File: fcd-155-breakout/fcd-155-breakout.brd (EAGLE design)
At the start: 52 x 63.2 mm, 2 parts, among them X1 RJ45-8X-E5908

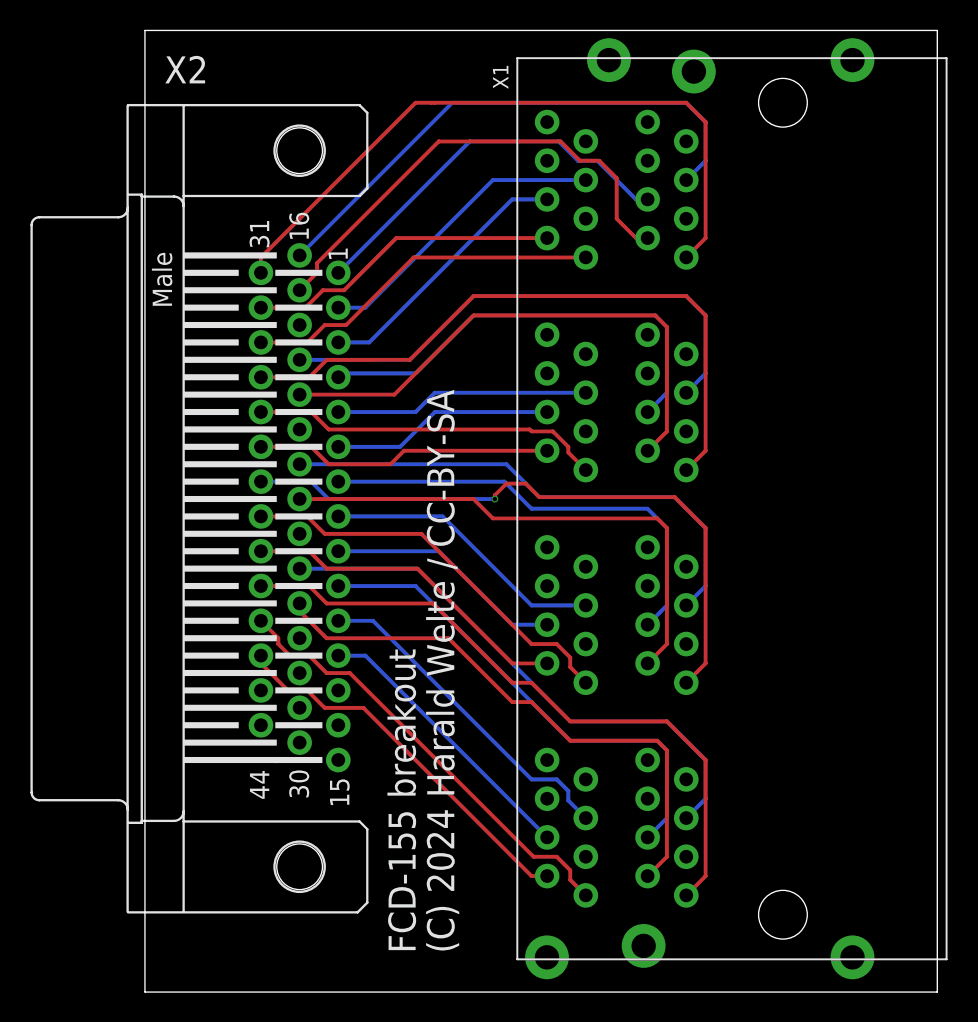
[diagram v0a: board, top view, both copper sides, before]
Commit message: fcd-155-breakout: Fix pin-out for even numbered ports
Related: OS#6678
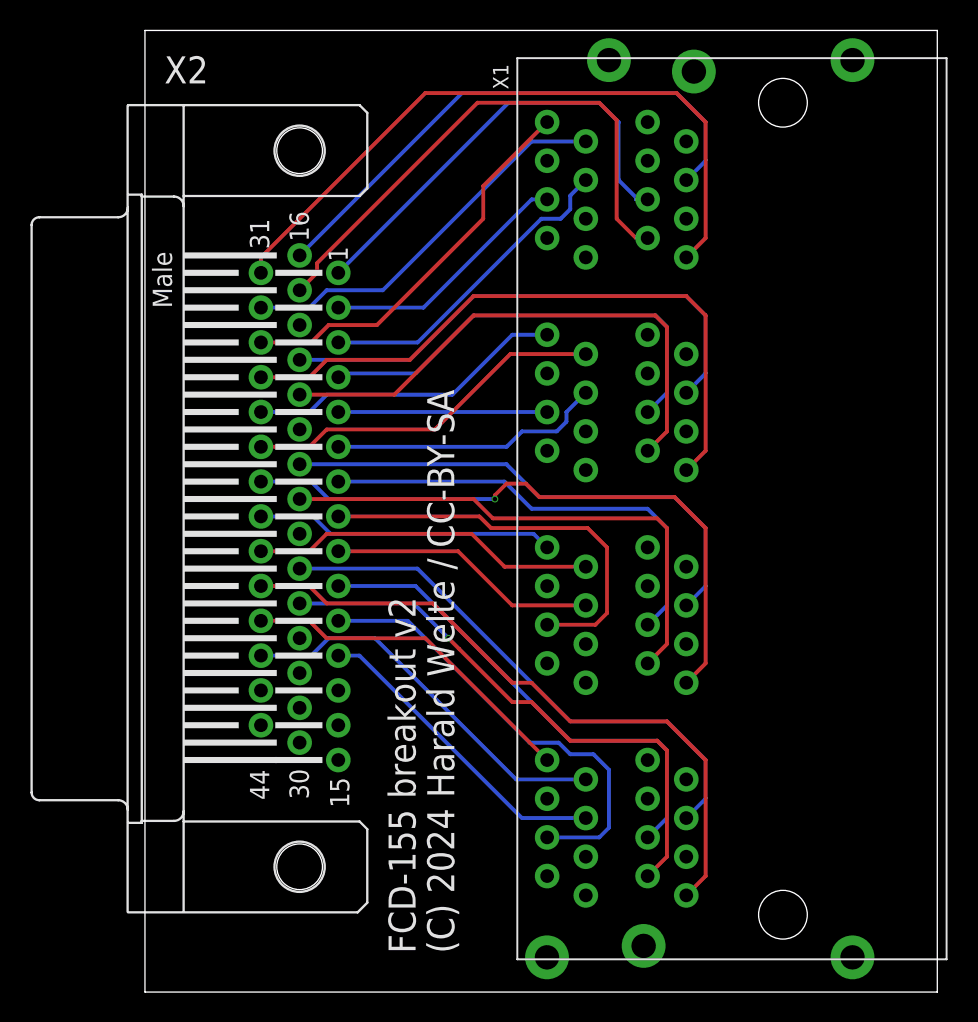
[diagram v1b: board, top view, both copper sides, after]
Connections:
- net CH2_RX_N: now also X1.D1; no longer X1.DU1
- net CH2_RX_P: now also X1.D2; no longer X1.DU2
- net CH2_TX_N: now also X1.D4; no longer X1.DU4
- net CH2_TX_P: now also X1.D5; no longer X1.DU5
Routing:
- net CH6_TX_P: track 18.7 -> 27.1 mm
- net CH8_TX_P: track 22.0 -> 30.0 mm
- net CH8_RX_N: track 29.4 -> 22.6 mm
- net CH6_RX_N: track 26.2 -> 19.6 mm
- net CH2_RX_P: track 20.7 -> 25.9 mm
- net CH1_TX_N: track 25.5 -> 29.9 mm
- net CH1_RX_P: track 31.5 -> 35.8 mm
- net CH4_RX_P: track 19.6 -> 23.9 mm
- net CH2_TX_N: track 17.6 -> 21.2 mm
- net CH4_TX_N: track 14.9 -> 18.1 mm
- net CH2_TX_P: track 19.7 -> 16.7 mm
- net CH4_TX_P: track 16.8 -> 13.7 mm
- net CH2_RX_N: track 23.7 -> 26.1 mm
- net CH4_RX_N: track 23.1 -> 20.9 mm
- net CH8_TX_N: track 18.7 -> 20.7 mm
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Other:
- board text added: "FCD-155 breakout v2"
- board text removed: "FCD-155 breakout"
